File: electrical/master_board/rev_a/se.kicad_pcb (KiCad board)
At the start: 2 copper layers, 66.2 x 45.2 mm, 7 parts, among them CN107 BRIDGE_SE_OUTER;M1x8

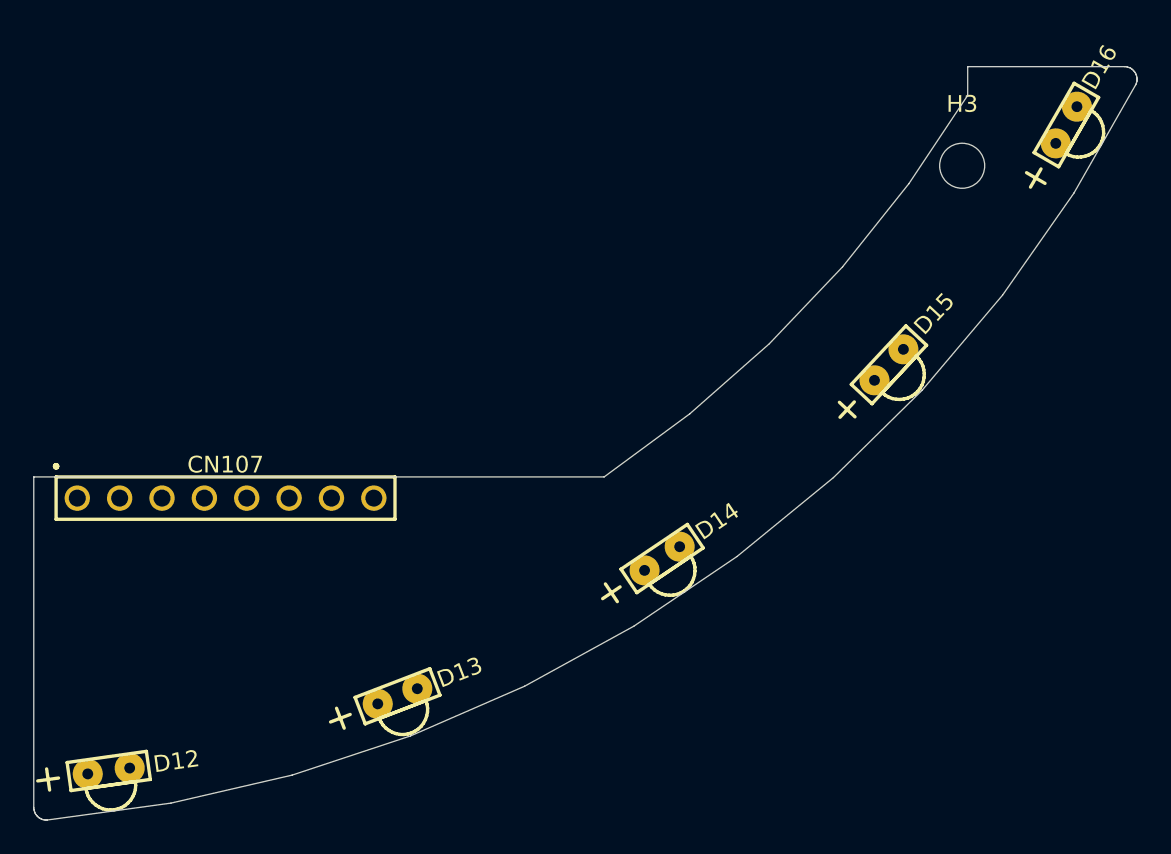
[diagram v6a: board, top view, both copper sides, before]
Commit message: The four corner boards ne/nw/se/sw are now zoned.
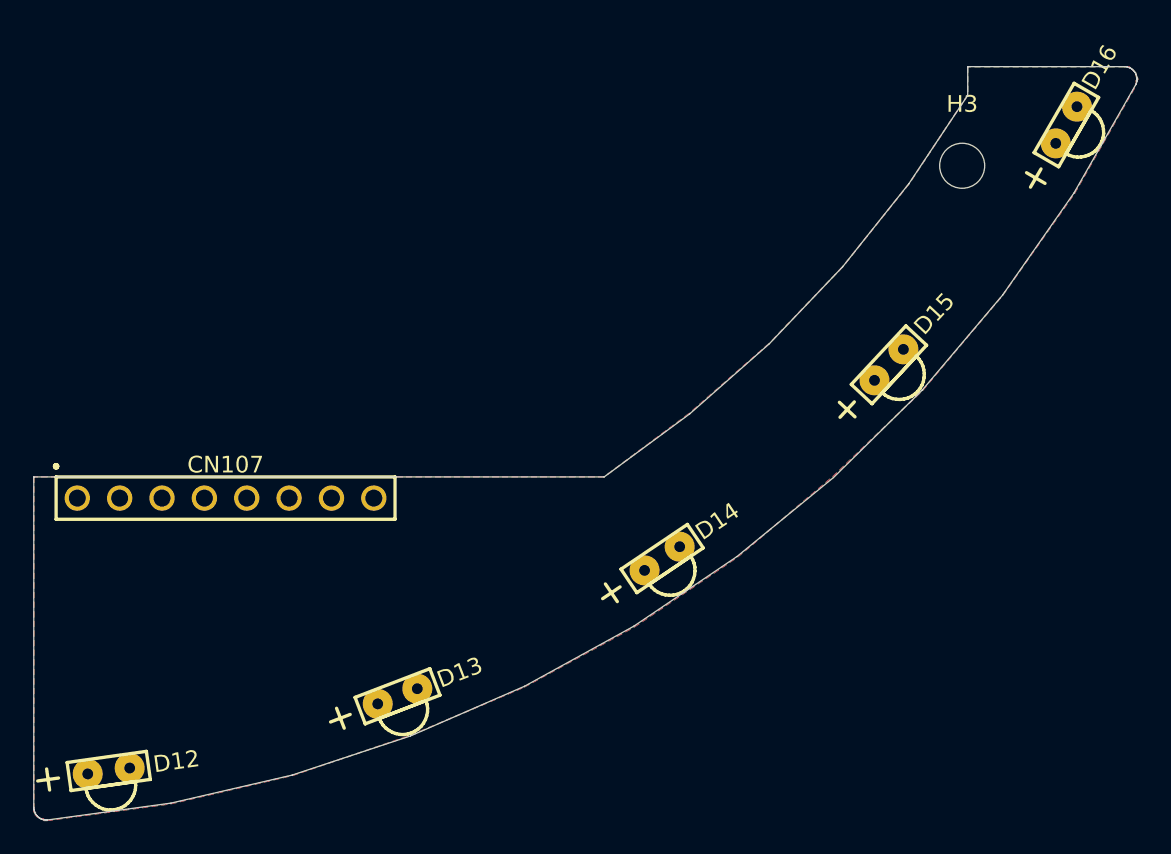
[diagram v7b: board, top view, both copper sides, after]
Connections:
- net Net-(CN107-Pad1) renamed /GND
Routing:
- added copper zone on B.Cu, net /GND
- added copper zone on F.Cu, net /GND
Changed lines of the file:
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@@
   (net 6 "Net-(CN107-Pad3)")
   (net 7 "Net-(CN107-Pad2)")
-  (net 8 "Net-(CN107-Pad1)")
+  (net 8 /GND)
   (net_class Default "This is the default net class."
     (clearance 0.2)
@@
     (uvia_dia 0.3)
     (uvia_drill 0.1)
-    (add_net "Net-(CN107-Pad1)")
+    (add_net /GND)
     (add_net "Net-(CN107-Pad2)")
     (add_net "Net-(CN107-Pad3)")
@@
       (net 7 "Net-(CN107-Pad2)"))
     (pad 1 thru_hole circle (at -8.89 0) (size 1.52 1.52) (drill 1.02) (layers *.Cu *.Mask)
-      (net 8 "Net-(CN107-Pad1)"))
+      (net 8 /GND))
   )
   (module HR2:LED_GRNRA (layer F.Cu)
@@
   (gr_line (start 145.83 156.82) (end 140.7 160.6) (layer Edge.Cuts) (width 0.05))
   (gr_line (start 140.7 160.6) (end 106.5 160.6) (layer Edge.Cuts) (width 0.05))
+  (zone (net 8) (net_name /GND) (layer F.Cu) (hatch edge 0.508)
+    (connect_pads (clearance 0.508))
+    (min_thickness 0.254)
+    (fill yes (arc_segments 32) (thermal_gap 0.508) (thermal_bridge_width 0.508))
+    (polygon
+      (pts
+        (xy 106.5 160.6) (xy 106.5 180.4) (xy 106.5 180.5) (xy 106.5 180.6)
+        (xy 106.5 180.6) (xy 106.5 180.7) (xy 106.6 180.7) (xy 106.6 180.8)
+        (xy 106.6 180.9) (xy 106.7 180.9) (xy 106.7 181) (xy 106.8 181)
+        (xy 106.8 181) (xy 106.9 181.1) (xy 106.9 181.1) (xy 107 181.1)
+        (xy 107.1 181.1) (xy 107.1 181.2) (xy 107.2 181.2) (xy 107.3 181.2)
+        (xy 107.3 181.2) (xy 107.3 181.2) (xy 114.7 180.2) (xy 122 178.5)
+        (xy 129.1 176.1) (xy 135.9 173.2) (xy 142.5 169.6) (xy 148.7 165.4)
+        (xy 154.4 160.6) (xy 159.8 155.4) (xy 164.6 149.7) (xy 168.9 143.6)
+        (xy 172.6 137.1) (xy 172.6 137) (xy 172.6 137) (xy 172.6 136.9)
+        (xy 172.6 136.8) (xy 172.7 136.8) (xy 172.7 136.7) (xy 172.6 136.6)
+        (xy 172.6 136.6) (xy 172.6 136.5) (xy 172.6 136.4) (xy 172.6 136.4)
+        (xy 172.5 136.3) (xy 172.5 136.3) (xy 172.4 136.2) (xy 172.4 136.2)
+        (xy 172.3 136.1) (xy 172.3 136.1) (xy 172.2 136.1) (xy 172.2 136)
+        (xy 172.1 136) (xy 172 136) (xy 172 136) (xy 171.9 136)
+        (xy 162.5 136) (xy 162.5 137.7) (xy 159 143) (xy 155 148)
+        (xy 150.6 152.6) (xy 145.8 156.8) (xy 140.7 160.6)
+      )
+    )
+  )
+  (zone (net 8) (net_name /GND) (layer B.Cu) (hatch edge 0.508)
+    (connect_pads (clearance 0.508))
+    (min_thickness 0.254)
+    (fill yes (arc_segments 32) (thermal_gap 0.508) (thermal_bridge_width 0.508))
+    (polygon
+      (pts
+        (xy 106.5 160.6) (xy 106.5 180.4) (xy 106.5 180.5) (xy 106.5 180.6)
+        (xy 106.5 180.6) (xy 106.5 180.7) (xy 106.6 180.7) (xy 106.6 180.8)
+        (xy 106.6 180.9) (xy 106.7 180.9) (xy 106.7 181) (xy 106.8 181)
+        (xy 106.8 181) (xy 106.9 181.1) (xy 106.9 181.1) (xy 107 181.1)
+        (xy 107.1 181.1) (xy 107.1 181.2) (xy 107.2 181.2) (xy 107.3 181.2)
+        (xy 107.3 181.2) (xy 107.3 181.2) (xy 114.7 180.2) (xy 122 178.5)
+        (xy 129.1 176.1) (xy 135.9 173.2) (xy 142.5 169.6) (xy 148.7 165.4)
+        (xy 154.4 160.6) (xy 159.8 155.4) (xy 164.6 149.7) (xy 168.9 143.6)
+        (xy 172.6 137.1) (xy 172.6 137) (xy 172.6 137) (xy 172.6 136.9)
+        (xy 172.6 136.8) (xy 172.7 136.8) (xy 172.7 136.7) (xy 172.6 136.6)
+        (xy 172.6 136.6) (xy 172.6 136.5) (xy 172.6 136.4) (xy 172.6 136.4)
+        (xy 172.5 136.3) (xy 172.5 136.3) (xy 172.4 136.2) (xy 172.4 136.2)
+        (xy 172.3 136.1) (xy 172.3 136.1) (xy 172.2 136.1) (xy 172.2 136)
+        (xy 172.1 136) (xy 172 136) (xy 172 136) (xy 171.9 136)
+        (xy 162.5 136) (xy 162.5 137.7) (xy 159 143) (xy 155 148)
+        (xy 150.6 152.6) (xy 145.8 156.8) (xy 140.7 160.6)
+      )
+    )
+  )
 )
